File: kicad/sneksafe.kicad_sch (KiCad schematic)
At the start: 13 parts, among them J1 BME280, J2 Screw_Terminal_01x06, J3 Screw_Terminal_01x03, K1 CPC40055ST, K2 CPC40055ST, U1 ESP32-DEVKITC-32D

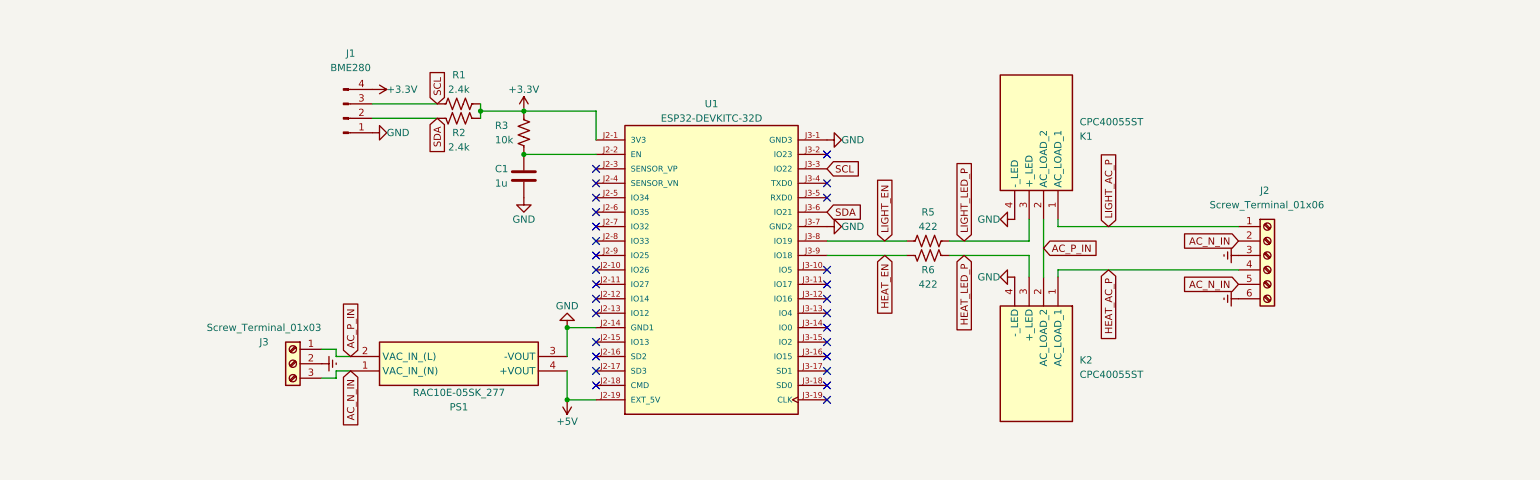
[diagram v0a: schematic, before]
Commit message: pcb: prepare for CI-generated BOM
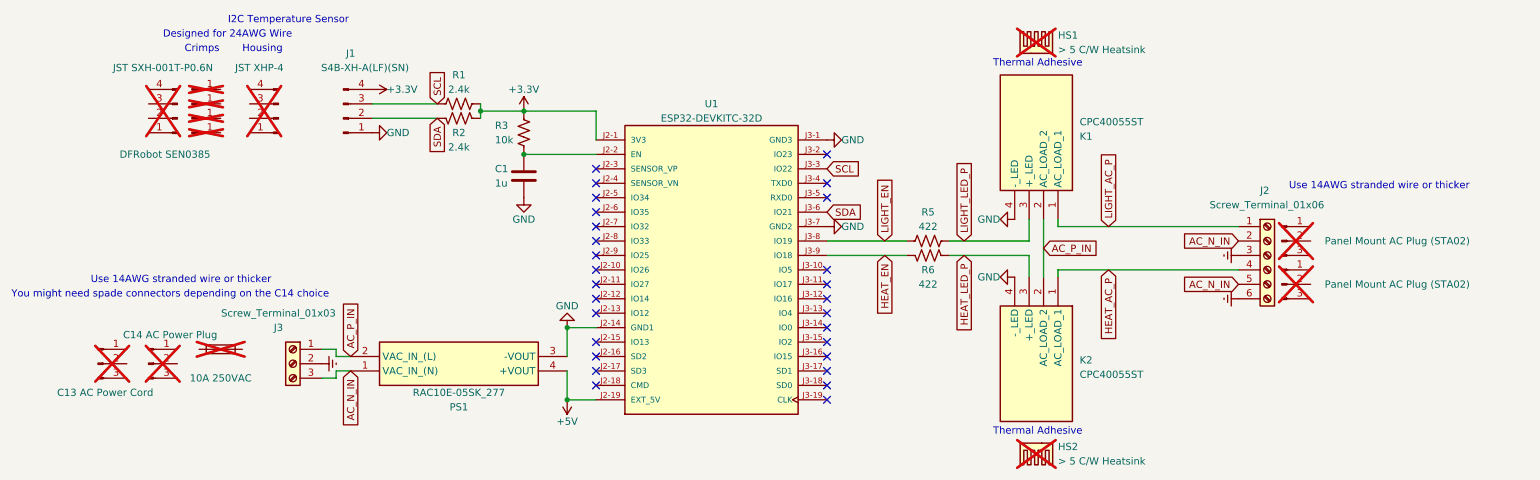
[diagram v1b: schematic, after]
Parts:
- added ACCord1: C13 AC Power Cord, symbol Connector:Conn_01x03_Pin
- added ACFuse1: 10A 250VAC, symbol Device:Fuse
- added ACOutput1, ACOutput2: Panel Mount AC Plug (STA02), symbol Connector:Conn_01x03_Pin
- added ACPlug1: C14 AC Power Plug, symbol Connector:Conn_01x03_Pin
- added HS1, HS2: > 5 C/W Heatsink, symbol Mechanical:Heatsink
- added TempPlug1: JST XHP-4, symbol Connector:Conn_01x04_Pin
- added TempPlugCrimp1, TempPlugCrimp2, TempPlugCrimp3, TempPlugCrimp4: JST SXH-001T-P0.6N, symbol Connector:Conn_01x01_Pin
- added TempSensor1: DFRobot SEN0385, symbol Connector:Conn_01x04_Pin
- C1: Manufacturer_Name (none) -> Murata; Manufacturer_Part_Number (none) -> GRM31CR72A105KA01K; Price (none) -> $0.78; Product Link (none) -> https://www.mouser.com/ProductDetail/81-GRM31CR72A105KA1K
- J1: value BME280 -> S4B-XH-A(LF)(SN); Manufacturer_Name (none) -> JST; Manufacturer_Part_Number (none) -> S4B-XH-A(LF)(SN); Price (none) -> $0.27; Product Link (none) -> https://www.digikey.com/en/products/detail/jst-sales-americ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
- J2: Manufacturer_Name (none) -> Phoenix Contact; Manufacturer_Part_Number (none) -> 1713969; Price (none) -> $5.84; Product Link (none) -> https://www.mouser.com/ProductDetail/651-1713969
- J3: Manufacturer_Name (none) -> Phoenix Contact; Manufacturer_Part_Number (none) -> 1714968; Price (none) -> $2.79; Product Link (none) -> https://www.mouser.com/ProductDetail/651-1714968
- K1, K2: Manufacturer_Name LITTELFUSE -> Littelfuse; Price (none) -> $13.35; Product Link (none) -> https://www.mouser.com/ProductDetail/849-CPC40055ST
- PS1: Price (none) -> $9.55; Product Link (none) -> https://www.mouser.com/ProductDetail/919-RAC10E-05SK-277
- R1, R2: Manufacturer_Name (none) -> Panasonic; Manufacturer_Part_Number (none) -> ERA-8AEB242V; Price (none) -> $0.64; Product Link (none) -> https://www.mouser.com/ProductDetail/667-ERA-8AEB242V
- R3: Manufacturer_Name (none) -> Panasonic; Manufacturer_Part_Number (none) -> ERA-8AEB103V; Price (none) -> $0.70; Product Link (none) -> https://www.mouser.com/ProductDetail/667-ERA-8AEB103V
- R5, R6: Manufacturer_Name (none) -> Panasonic; Manufacturer_Part_Number (none) -> ERA-8AEB4220V; Price (none) -> $0.66; Product Link (none) -> https://www.mouser.com/ProductDetail/667-ERA-8AEB4220V
- U1: Manufacturer_Name (none) -> Espressif Systems; Manufacturer_Part_Number (none) -> ESP32-DevKitC-32E; Price (none) -> $10.00; Product Link (none) -> https://www.mouser.com/ProductDetail/356-ESP32-DEVKITC32E
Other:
- note added: "Crimps"
- note added: "Designed for 24AWG Wire"
- note added: "Housing"
- note added: "I2C Temperature Sensor"
- note added: "Thermal Adhesive"
- note added: "Use 14AWG stranded wire or thicker"
- note added: "You might need spade connectors depending on the C14 choice"
